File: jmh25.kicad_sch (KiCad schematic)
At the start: 27 parts, among them J1 FBNAB2470ZG110, J2 39-28-1103 MOLEX

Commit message: Upgrade to KiCad 9.
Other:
- title: Napájecí zdroj kolejišť KMŽ/LRKV 2024/2025 -> Napájecí zdroj kolejišť JMH-25
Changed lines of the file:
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@@
 (kicad_sch
-	(version 20231120)
+	(version 20250114)
 	(generator "eeschema")
-	(generator_version "8.0")
+	(generator_version "9.0")
 	(paper "A4")
 	(title_block
-		(title "Napájecí zdroj kolejišť KMŽ/LRKV 2024/2025")
-		(date "2025-01-01")
+		(title "Napájecí zdroj kolejišť JMH-25")
+		(date "2025-03-28")
 		(rev "1.0")
 		(company "Jan Horáček, Miroslav Horáček")
@@
 		(comment 2 "Laboratoř řízení kolejových vozidel MENDELU")
 	)
+	(text "Uzemnění skříně"
+		(exclude_from_sim no)
+		(at 48.26 66.04 0)
+		(effects
+			(font
+				(size 1.27 1.27)
+			)
+		)
+	)
+	(text "Doutnavka LA1\nje součástí\nspínače CB1"
+		(exclude_from_sim no)
+		(at 76.2 107.95 0)
+		(effects
+			(font
+				(size 1.27 1.27)
+			)
+		)
+	)
+	(text "Omezení pro návrh:\n* Indikační LED musí být za pojistkou (aby indikovala stav pojistky).\n* Tlačítko by nejspíš mělo být před pojistkou (aby se dala měnit pojistka za vypnutého zdroje).\n\nVšechny silové vodiče 1.0 mm², PS1-MES1 1.5 mm²."
+		(exclude_from_sim no)
+		(at 35.56 175.26 0)
+		(effects
+			(font
+				(size 1.27 1.27)
+			)
+			(justify left top)
+		)
+	)
+	(text "Napájet přímo\nz výstupu PS2"
+		(exclude_from_sim no)
+		(at 139.7 120.65 0)
+		(effects
+			(font
+				(size 1.27 1.27)
+			)
+		)
+	)
+	(text "Síťový filtr\nje součástí J1"
+		(exclude_from_sim no)
+		(at 25.4 101.6 0)
+		(effects
+			(font
+				(size 1.27 1.27)
+			)
+		)
+	)
+	(text "Napájet přímo\nz výstupu PS3"
+		(exclude_from_sim no)
+		(at 139.7 146.05 0)
+		(effects
+			(font
+				(size 1.27 1.27)
+			)
+		)
+	)
+	(text "Napájet přímo\nz výstupu PS1"
+		(exclude_from_sim no)
+		(at 139.7 44.45 0)
+		(effects
+			(font
+				(size 1.27 1.27)
+			)
+		)
+	)
 	(junction
 		(at 85.09 91.44)
@@
 		)
 	)
-	(text "Uzemnění skříně"
-		(exclude_from_sim no)
-		(at 48.26 66.04 0)
-		(effects
-			(font
-				(size 1.27 1.27)
-			)
-		)
-	)
-	(text "Doutnavka LA1\nje součástí\nspínače CB1"
-		(exclude_from_sim no)
-		(at 76.2 107.95 0)
-		(effects
-			(font
-				(size 1.27 1.27)
-			)
-		)
-	)
-	(text "Omezení pro návrh:\n* Indikační LED musí být za pojistkou (aby indikovala stav pojistky).\n* Tlačítko by nejspíš mělo být před pojistkou (aby se dala měnit pojistka za vypnutého zdroje).\n\nVšechny silové vodiče 1.0 mm², PS1-MES1 1.5 mm²."
-		(exclude_from_sim no)
-		(at 35.56 175.26 0)
-		(effects
-			(font
-				(size 1.27 1.27)
-			)
-			(justify left top)
-		)
-	)
-	(text "Napájet přímo\nz výstupu PS2"
-		(exclude_from_sim no)
-		(at 139.7 120.65 0)
-		(effects
-			(font
-				(size 1.27 1.27)
-			)
-		)
-	)
-	(text "Síťový filtr\nje součástí J1"
-		(exclude_from_sim no)
-		(at 25.4 101.6 0)
-		(effects
-			(font
-				(size 1.27 1.27)
-			)
-		)
-	)
-	(text "Napájet přímo\nz výstupu PS3"
-		(exclude_from_sim no)
-		(at 139.7 146.05 0)
-		(effects
-			(font
-				(size 1.27 1.27)
-			)
-		)
-	)
-	(text "Napájet přímo\nz výstupu PS1"
-		(exclude_from_sim no)
-		(at 139.7 44.45 0)
-		(effects
-			(font
-				(size 1.27 1.27)
-			)
-		)
-	)
 	(label "GND"
 		(at 200.66 76.2 0)
-		(fields_autoplaced yes)
 		(effects
 			(font
@@
 	(label "GND-SWITCH"
 		(at 260.35 91.44 0)
-		(fields_autoplaced yes)
 		(effects
 			(font
@@
 	(label "GND-ACC"
 		(at 260.35 86.36 0)
-		(fields_autoplaced yes)
 		(effects
 			(font
@@
 	(label "SWITCH"
 		(at 247.65 91.44 180)
-		(fields_autoplaced yes)
 		(effects
 			(font
@@
 	(label "MTB"
 		(at 260.35 83.82 0)
-		(fields_autoplaced yes)
 		(effects
 			(font
@@
 	(label "ACC"
 		(at 247.65 86.36 180)
-		(fields_autoplaced yes)
 		(effects
 			(font
@@
 	(label "GND-DSC"
 		(at 200.66 152.4 0)
-		(fields_autoplaced yes)
 		(effects
 			(font
@@
 	(label "GND-SWITCH"
 		(at 200.66 50.8 0)
-		(fields_autoplaced yes)
 		(effects
 			(font
@@
 	(label "DSC"
 		(at 200.66 139.7 0)
-		(fields_autoplaced yes)
 		(effects
 			(font
@@
 	(label "MTB"
 		(at 200.66 63.5 0)
-		(fields_autoplaced yes)
 		(effects
 			(font
@@
 	(label "DSC"
 		(at 247.65 88.9 180)
-		(fields_autoplaced yes)
 		(effects
 			(font
@@
 	(label "BOOST+"
 		(at 200.66 114.3 0)
-		(fields_autoplaced yes)
 		(effects
 			(font
@@
 	(label "ACC"
 		(at 200.66 88.9 0)
-		(fields_autoplaced yes)
 		(effects
 			(font
@@
 	(label "GND-ACC"
 		(at 200.66 101.6 0)
-		(fields_autoplaced yes)
 		(effects
 			(font
@@
 	(label "GND-DSC"
 		(at 260.35 88.9 0)
-		(fields_autoplaced yes)
 		(effects
 			(font
@@
 	(label "SWITCH"
 		(at 200.66 38.1 0)
-		(fields_autoplaced yes)
 		(effects
 			(font
@@
 	(label "BOOST-"
 		(at 200.66 127 0)
-		(fields_autoplaced yes)
 		(effects
 			(font
@@
 	(label "GND"
 		(at 247.65 83.82 180)
-		(fields_autoplaced yes)
 		(effects
 			(font
@@
 	(label "BOOST-"
 		(at 260.35 93.98 0)
-		(fields_autoplaced yes)
 		(effects
 			(font
@@
 	(label "BOOST+"
 		(at 247.65 93.98 180)
-		(fields_autoplaced yes)
 		(effects
 			(font
@@
 			)
 		)
+		(property "Sim.Pins" "1=K 2=A"
+			(at 215.9 95.25 0)
+			(effects
+				(font
+					(size 1.27 1.27)
+				)
+				(hide yes)
+			)
+		)
 		(pin "2"
 		)
@@
 		(at 43.18 58.42 0)
 		(unit 1)
-		(exclude_from_sim yes)
+		(exclude_from_sim no)
 		(in_bom yes)
 		(on_board yes)
@@
 			)
 		)
+		(property "Sim.Pins" "1=K 2=A"
+			(at 215.9 120.65 0)
+			(effects
+				(font
+					(size 1.27 1.27)
+				)
+				(hide yes)
+			)
+		)
 		(pin "2"
 		)
@@
 			)
 		)
+		(property "Sim.Pins" "1=K 2=A"
+			(at 215.9 44.45 0)
+			(effects
+				(font
+					(size 1.27 1.27)
+				)
+				(hide yes)
+			)
+		)
 		(pin "2"
 		)
@@
 			)
 		)
+		(property "Sim.Pins" "1=K 2=A"
+			(at 215.9 69.85 0)
+			(effects
+				(font
+					(size 1.27 1.27)
+				)
+				(hide yes)
+			)
+		)
 		(pin "2"
 		)
@@
 			)
 		)
+		(property "Sim.Pins" "1=K 2=A"
+			(at 215.9 146.05 0)
+			(effects
+				(font
+					(size 1.27 1.27)
+				)
+				(hide yes)
+			)
+		)
 		(pin "2"
 		)
@@
 		)
 	)
+	(embedded_fonts no)
 )

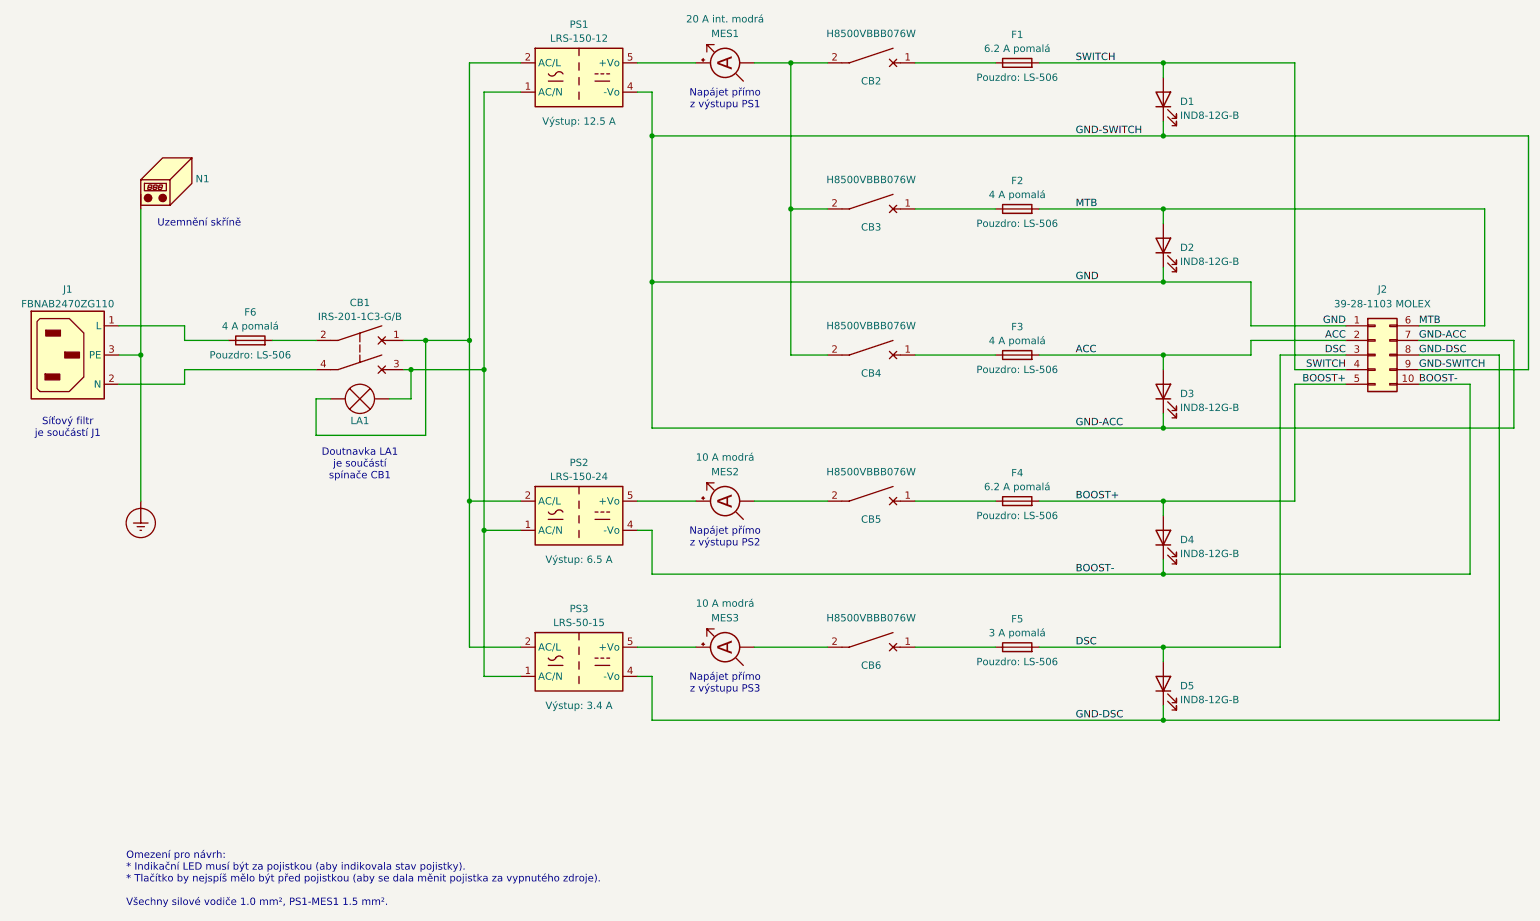
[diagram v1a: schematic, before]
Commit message: Ampermetry musi byt v zaporne vervi.
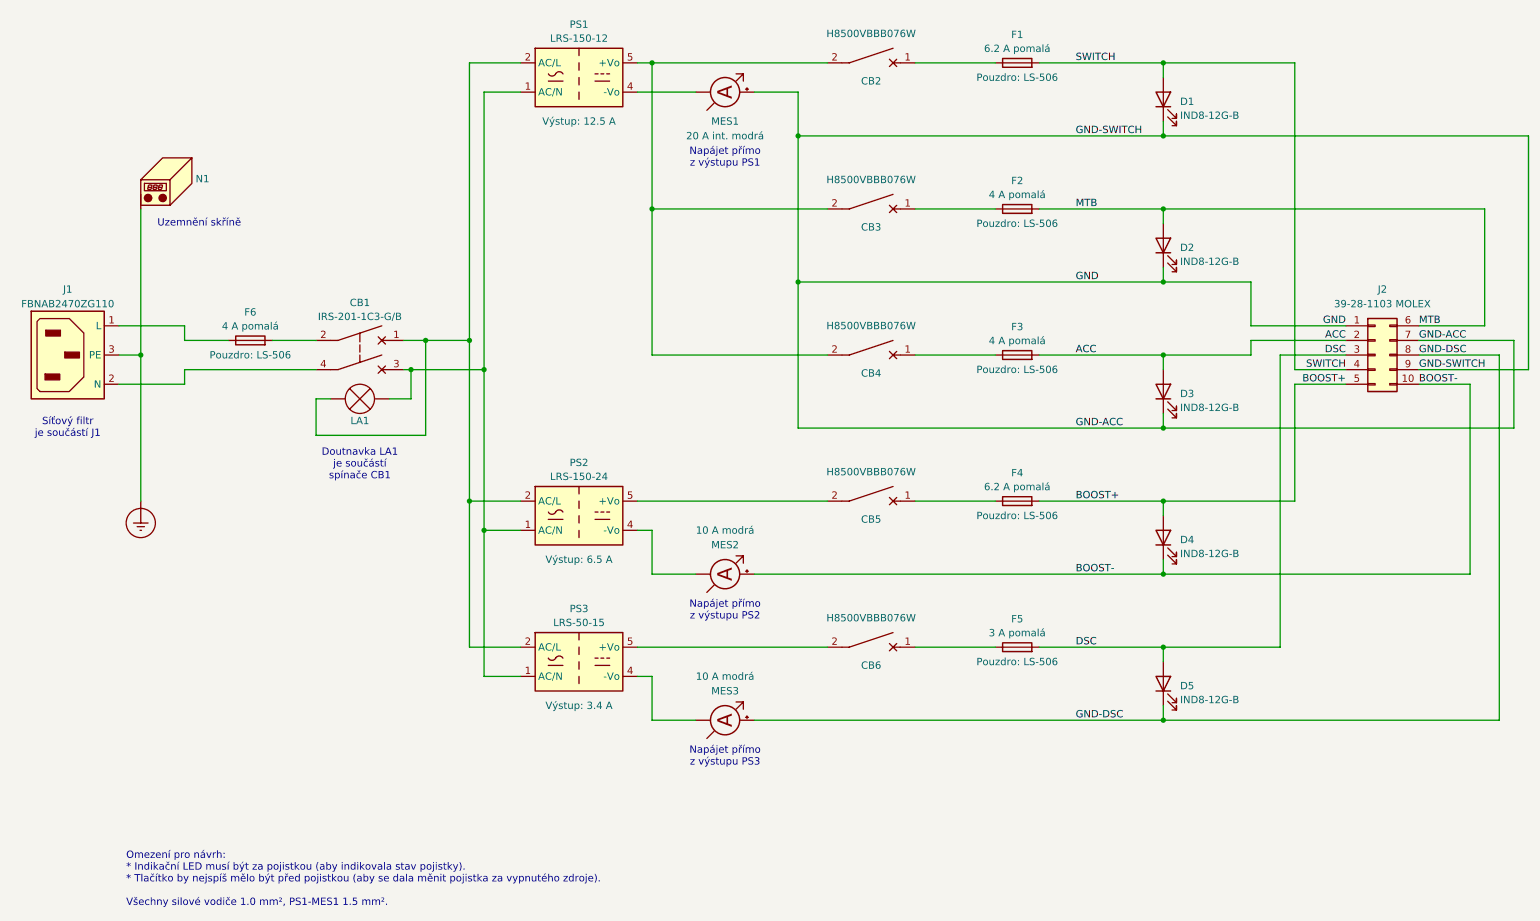
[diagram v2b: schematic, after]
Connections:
- net BOOST-: now also MES2.2 (+); no longer PS2.4 (-Vo)
- net GND: now also MES1.2 (+); no longer PS1.4 (-Vo)
- net GND-DSC: now also MES3.2 (+); no longer PS3.4 (-Vo)
- net at CB6.2: now also PS3.5 (+Vo); no longer MES3.1 (-)
- net at CB2.2, CB3.2, CB4.2: now also PS1.5 (+Vo); no longer MES1.1 (-)
- net at PS2.5 (+Vo): now also CB5.2; no longer MES2.2 (+)
- net at MES2.1 (-): now also PS2.4 (-Vo); no longer CB5.2
- new net: MES1.1 (-), PS1.4 (-Vo)
- new net: MES3.1 (-), PS3.4 (-Vo)
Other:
- moved on the sheet: MES1, MES2, MES3
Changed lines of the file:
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@@
 		(title "Napájecí zdroj kolejišť JMH-25")
 		(date "2025-03-28")
-		(rev "1.0")
+		(rev "1.1")
 		(company "Jan Horáček, Miroslav Horáček")
 		(comment 1 "Klub modelářů železnic Brno I, p. s.")
@@
 	(text "Napájet přímo\nz výstupu PS2"
 		(exclude_from_sim no)
-		(at 139.7 120.65 0)
+		(at 139.7 133.35 0)
 		(effects
 			(font
@@
 	(text "Napájet přímo\nz výstupu PS3"
 		(exclude_from_sim no)
-		(at 139.7 146.05 0)
+		(at 139.7 158.75 0)
 		(effects
 			(font
@@
 	(text "Napájet přímo\nz výstupu PS1"
 		(exclude_from_sim no)
-		(at 139.7 44.45 0)
+		(at 139.7 54.61 0)
 		(effects
 			(font
@@
 	)
 	(junction
-		(at 127 76.2)
+		(at 152.4 76.2)
 		(diameter 0)
 		(color 0 0 0 0)
 	)
 	(junction
-		(at 127 50.8)
+		(at 152.4 50.8)
 		(diameter 0)
 		(color 0 0 0 0)
@@
 	)
 	(junction
-		(at 151.13 38.1)
+		(at 127 38.1)
 		(diameter 0)
 		(color 0 0 0 0)
@@
 	)
 	(junction
-		(at 151.13 63.5)
+		(at 127 63.5)
 		(diameter 0)
 		(color 0 0 0 0)
@@
 	(wire
 		(pts
-			(xy 151.13 63.5) (xy 151.13 88.9)
+			(xy 127 63.5) (xy 127 88.9)
 		)
 		(stroke
@@
 	(wire
 		(pts
-			(xy 124.46 38.1) (xy 134.62 38.1)
-		)
-		(stroke
-			(width 0)
-			(type default)
-		)
-	)
-	(wire
-		(pts
-			(xy 127 76.2) (xy 127 101.6)
+			(xy 124.46 38.1) (xy 127 38.1)
+		)
+		(stroke
+			(width 0)
+			(type default)
+		)
+	)
+	(wire
+		(pts
+			(xy 152.4 76.2) (xy 152.4 101.6)
 		)
 		(stroke
@@
 	(wire
 		(pts
-			(xy 144.78 139.7) (xy 157.48 139.7)
+			(xy 144.78 127) (xy 215.9 127)
 		)
 		(stroke
@@
 	(wire
 		(pts
-			(xy 127 50.8) (xy 127 76.2)
+			(xy 152.4 50.8) (xy 152.4 76.2)
 		)
 		(stroke
@@
 	(wire
 		(pts
+			(xy 144.78 43.18) (xy 152.4 43.18)
+		)
+		(stroke
+			(width 0)
+			(type default)
+		)
+	)
+	(wire
+		(pts
 			(xy 215.9 63.5) (xy 271.78 63.5)
 		)
@@
 	(wire
 		(pts
-			(xy 127 101.6) (xy 215.9 101.6)
+			(xy 152.4 101.6) (xy 215.9 101.6)
 		)
 		(stroke
@@
 	(wire
 		(pts
-			(xy 151.13 63.5) (xy 157.48 63.5)
+			(xy 127 63.5) (xy 157.48 63.5)
 		)
 		(stroke
@@
 	(wire
 		(pts
-			(xy 127 152.4) (xy 215.9 152.4)
+			(xy 127 152.4) (xy 134.62 152.4)
 		)
 		(stroke
@@
 	(wire
 		(pts
-			(xy 127 76.2) (xy 215.9 76.2)
+			(xy 152.4 76.2) (xy 215.9 76.2)
 		)
 		(stroke
@@
 	(wire
 		(pts
-			(xy 127 50.8) (xy 215.9 50.8)
-		)
-		(stroke
-			(width 0)
-			(type default)
-		)
-	)
-	(wire
-		(pts
-			(xy 124.46 139.7) (xy 134.62 139.7)
+			(xy 152.4 50.8) (xy 215.9 50.8)
+		)
+		(stroke
+			(width 0)
+			(type default)
+		)
+	)
+	(wire
+		(pts
+			(xy 124.46 139.7) (xy 157.48 139.7)
 		)
 		(stroke
@@
 	(wire
 		(pts
-			(xy 144.78 38.1) (xy 151.13 38.1)
-		)
-		(stroke
-			(width 0)
-			(type default)
-		)
-	)
-	(wire
-		(pts
 			(xy 260.35 88.9) (xy 274.32 88.9)
 		)
@@
 	(wire
 		(pts
-			(xy 151.13 38.1) (xy 157.48 38.1)
+			(xy 127 38.1) (xy 157.48 38.1)
 		)
 		(stroke
@@
 	(wire
 		(pts
-			(xy 124.46 43.18) (xy 127 43.18)
+			(xy 124.46 43.18) (xy 134.62 43.18)
 		)
 		(stroke
@@
 	(wire
 		(pts
-			(xy 151.13 38.1) (xy 151.13 63.5)
+			(xy 127 38.1) (xy 127 63.5)
+		)
+		(stroke
+			(width 0)
+			(type default)
+		)
+	)
+	(wire
+		(pts
+			(xy 144.78 152.4) (xy 215.9 152.4)
 		)
 		(stroke
@@
 	(wire
 		(pts
-			(xy 151.13 88.9) (xy 157.48 88.9)
+			(xy 127 88.9) (xy 157.48 88.9)
 		)
 		(stroke
@@
 	(wire
 		(pts
-			(xy 144.78 114.3) (xy 157.48 114.3)
-		)
-		(stroke
-			(width 0)
-			(type default)
-		)
-	)
-	(wire
-		(pts
-			(xy 127 43.18) (xy 127 50.8)
-		)
-		(stroke
-			(width 0)
-			(type default)
-		)
-	)
-	(wire
-		(pts
-			(xy 124.46 114.3) (xy 134.62 114.3)
+			(xy 152.4 43.18) (xy 152.4 50.8)
+		)
+		(stroke
+			(width 0)
+			(type default)
+		)
+	)
+	(wire
+		(pts
+			(xy 124.46 114.3) (xy 157.48 114.3)
 		)
 		(stroke
@@
 	(wire
 		(pts
-			(xy 127 127) (xy 215.9 127)
+			(xy 127 127) (xy 134.62 127)
 		)
 		(stroke
@@
 	(symbol
 		(lib_id "Device:Ammeter_DC")
-		(at 139.7 114.3 90)
+		(at 139.7 127 270)
+		(mirror x)
 		(unit 1)
 		(exclude_from_sim no)
@@
 		(dnp no)
 		(property "Reference" "MES2"
-			(at 139.7 109.22 90)
+			(at 139.7 121.92 90)
 			(effects
 				(font
@@
 		)
 		(property "Value" "10 A modrá"
-			(at 139.7 106.68 90)
+			(at 139.7 119.38 90)
 			(effects
 				(font
@@
 		)
 		(property "Footprint" ""
-			(at 137.16 114.3 90)
+			(at 142.24 127 90)
 			(effects
 				(font
@@
 		)
 		(property "Datasheet" "~"
-			(at 137.16 114.3 90)
+			(at 142.24 127 90)
 			(effects
 				(font
@@
 		)
 		(property "Description" "DC ammeter"
-			(at 139.7 114.3 0)
+			(at 139.7 127 0)
 			(effects
 				(font
@@
 	(symbol
 		(lib_id "Device:Ammeter_DC")
-		(at 139.7 38.1 90)
+		(at 139.7 43.18 270)
+		(mirror x)
 		(unit 1)
 		(exclude_from_sim no)
@@
 		(dnp no)
 		(property "Reference" "MES1"
-			(at 139.7 33.02 90)
+			(at 139.7 48.26 90)
 			(effects
 				(font
@@
 		)
 		(property "Value" "20 A int. modrá"
-			(at 139.7 30.48 90)
+			(at 139.7 50.8 90)
 			(effects
 				(font
@@
 		)
 		(property "Footprint" ""
-			(at 137.16 38.1 90)
+			(at 142.24 43.18 90)
 			(effects
 				(font
@@
 		)
 		(property "Datasheet" "~"
-			(at 137.16 38.1 90)
+			(at 142.24 43.18 90)
 			(effects
 				(font
@@
 		)
 		(property "Description" "DC ammeter"
-			(at 139.7 38.1 0)
+			(at 139.7 43.18 0)
 			(effects
 				(font
@@
 	(symbol
 		(lib_id "Device:Ammeter_DC")
-		(at 139.7 139.7 90)
+		(at 139.7 152.4 270)
+		(mirror x)
 		(unit 1)
 		(exclude_from_sim no)
@@
 		(dnp no)
 		(property "Reference" "MES3"
-			(at 139.7 134.62 90)
+			(at 139.7 147.32 90)
 			(effects
 				(font
@@
 		)
 		(property "Value" "10 A modrá"
-			(at 139.7 132.08 90)
+			(at 139.7 144.78 90)
 			(effects
 				(font
@@
 		)
 		(property "Footprint" ""
-			(at 137.16 139.7 90)
+			(at 142.24 152.4 90)
 			(effects
 				(font
@@
 		)
 		(property "Datasheet" "~"
-			(at 137.16 139.7 90)
+			(at 142.24 152.4 90)
 			(effects
 				(font
@@
 		)
 		(property "Description" "DC ammeter"
-			(at 139.7 139.7 0)
-			(effects
-				(font
+			(at 139.7 152.4 0)
+			(effects
+				(font
